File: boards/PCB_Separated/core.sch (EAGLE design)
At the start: 5 parts, among them U1 STM32F10XRXT6

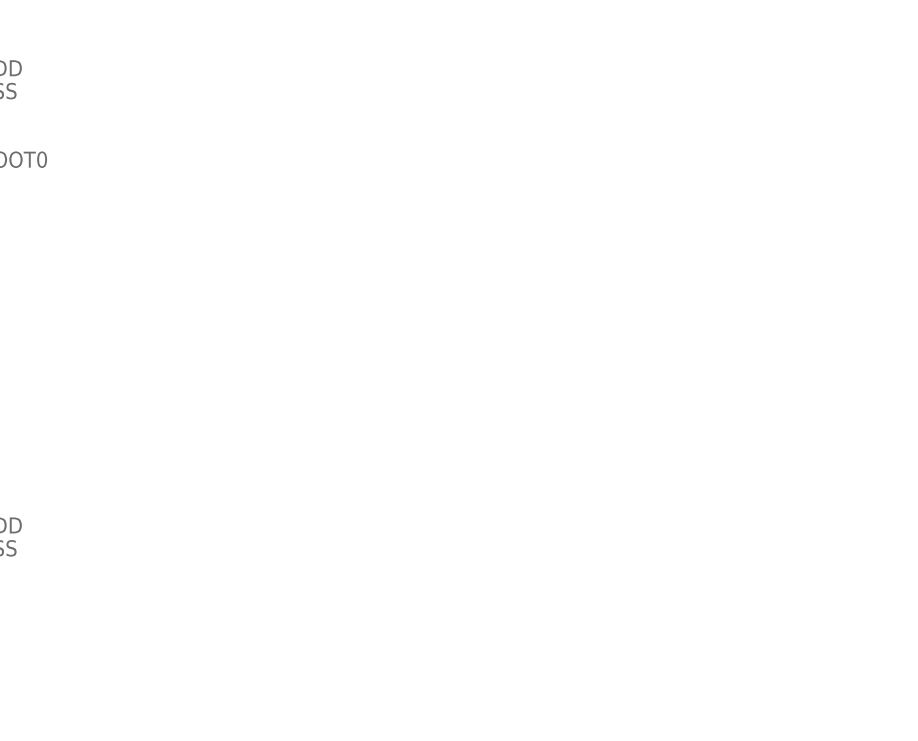
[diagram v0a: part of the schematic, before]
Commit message: Modify Board. Core and FTDI become one file
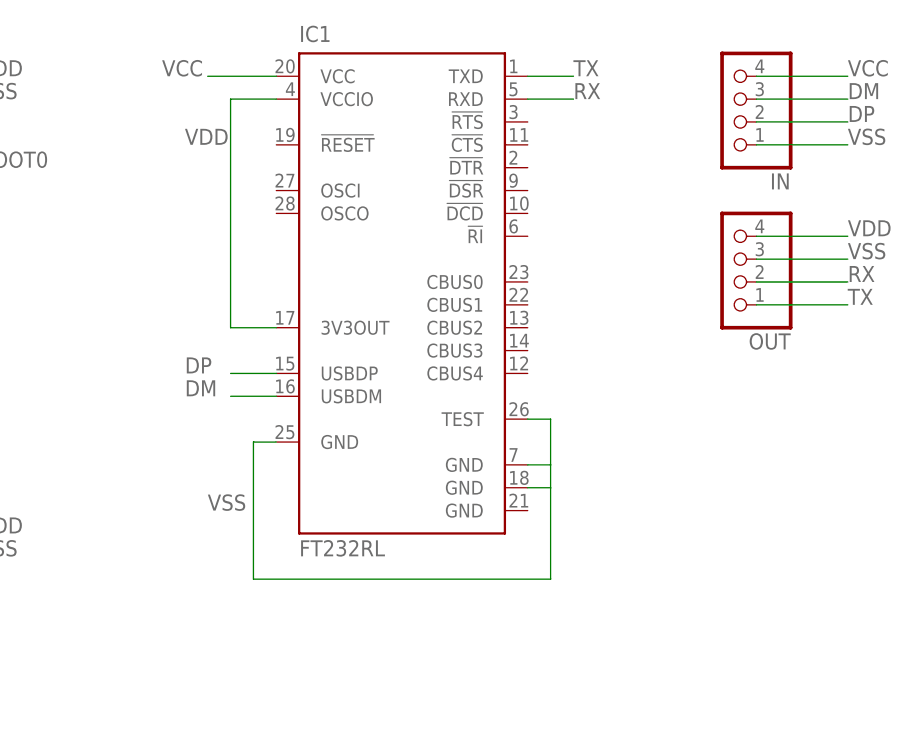
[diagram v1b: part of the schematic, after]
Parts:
- added IC1: FT232RL, ftdichip:FT232RL
- added IN, OUT: (no value), pinhead:PINHD-1X4
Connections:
- new net DM: IC1.USBDM, IN.3
- new net DP: IC1.USBDP, IN.2
- new net RX: IC1.RXD, OUT.2
- new net TX: IC1.TXD, OUT.1
- new net VCC: IC1.VCC, IN.4
- net VDD: now also IC1.3V3OUT, IC1.VCCIO, OUT.4
- net VSS: now also IC1.GND, IC1.GND@1, IC1.GND@A, IC1.TEST, IN.1, OUT.3
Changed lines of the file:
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@@
 <part name="JP3" library="pinhead" deviceset="PINHD-1X16" device=""/>
 <part name="JP4" library="pinhead" deviceset="PINHD-1X16" device=""/>
+<part name="IC1" library="ftdichip" deviceset="FT232R" device="L"/>
+<part name="IN" library="pinhead" deviceset="PINHD-1X4" device=""/>
+<part name="OUT" library="pinhead" deviceset="PINHD-1X4" device=""/>
 </parts>
 <sheets>
@@
 <instance part="JP3" gate="A" x="99.06" y="12.7" rot="R180"/>
 <instance part="JP4" gate="A" x="99.06" y="63.5" rot="R180"/>
+<instance part="IC1" gate="1" x="160.02" y="60.96"/>
+<instance part="IN" gate="A" x="198.12" y="81.28" rot="R180"/>
+<instance part="OUT" gate="A" x="198.12" y="63.5" rot="R180"/>
 </instances>
 <busses>
@@
 <label x="114.3" y="81.28" size="1.778" layer="95"/>
 </segment>
+<segment>
+<pinref part="IC1" gate="1" pin="GND@A"/>
+<wire x1="147.32" y1="43.18" x2="144.78" y2="43.18" width="0.1524" layer="91"/>
+<wire x1="144.78" y1="43.18" x2="144.78" y2="27.94" width="0.1524" layer="91"/>
+<wire x1="144.78" y1="27.94" x2="177.8" y2="27.94" width="0.1524" layer="91"/>
+<wire x1="177.8" y1="27.94" x2="177.8" y2="38.1" width="0.1524" layer="91"/>
+<pinref part="IC1" gate="1" pin="TEST"/>
+<wire x1="177.8" y1="38.1" x2="177.8" y2="40.64" width="0.1524" layer="91"/>
+<wire x1="177.8" y1="40.64" x2="177.8" y2="45.72" width="0.1524" layer="91"/>
+<wire x1="177.8" y1="45.72" x2="175.26" y2="45.72" width="0.1524" layer="91"/>
+<pinref part="IC1" gate="1" pin="GND"/>
+<wire x1="175.26" y1="40.64" x2="177.8" y2="40.64" width="0.1524" layer="91"/>
+<pinref part="IC1" gate="1" pin="GND@1"/>
+<wire x1="175.26" y1="38.1" x2="177.8" y2="38.1" width="0.1524" layer="91"/>
+<label x="139.7" y="35.56" size="1.778" layer="95"/>
+</segment>
+<segment>
+<pinref part="IN" gate="A" pin="1"/>
+<wire x1="200.66" y1="76.2" x2="210.82" y2="76.2" width="0.1524" layer="91"/>
+<label x="210.82" y="76.2" size="1.778" layer="95"/>
+</segment>
+<segment>
+<pinref part="OUT" gate="A" pin="3"/>
+<wire x1="200.66" y1="63.5" x2="210.82" y2="63.5" width="0.1524" layer="91"/>
+<label x="210.82" y="63.5" size="1.778" layer="95"/>
+</segment>
 </net>
 <net name="VDD" class="0">
@@
 <label x="114.3" y="83.82" size="1.778" layer="95"/>
 </segment>
+<segment>
+<pinref part="IC1" gate="1" pin="3V3OUT"/>
+<wire x1="147.32" y1="55.88" x2="142.24" y2="55.88" width="0.1524" layer="91"/>
+<wire x1="142.24" y1="55.88" x2="142.24" y2="81.28" width="0.1524" layer="91"/>
+<pinref part="IC1" gate="1" pin="VCCIO"/>
+<wire x1="142.24" y1="81.28" x2="147.32" y2="81.28" width="0.1524" layer="91"/>
+<label x="137.16" y="76.2" size="1.778" layer="95"/>
+</segment>
+<segment>
+<pinref part="OUT" gate="A" pin="4"/>
+<wire x1="200.66" y1="66.04" x2="210.82" y2="66.04" width="0.1524" layer="91"/>
+<label x="210.82" y="66.04" size="1.778" layer="95"/>
+</segment>
 </net>
 <net name="P14" class="0">
@@
 </segment>
 </net>
+<net name="VCC" class="0">
+<segment>
+<pinref part="IC1" gate="1" pin="VCC"/>
+<wire x1="147.32" y1="83.82" x2="139.7" y2="83.82" width="0.1524" layer="91"/>
+<label x="134.62" y="83.82" size="1.778" layer="95"/>
+</segment>
+<segment>
+<pinref part="IN" gate="A" pin="4"/>
+<wire x1="200.66" y1="83.82" x2="210.82" y2="83.82" width="0.1524" layer="91"/>
+<label x="210.82" y="83.82" size="1.778" layer="95"/>
+</segment>
+</net>
+<net name="DP" class="0">
+<segment>
+<pinref part="IC1" gate="1" pin="USBDP"/>
+<wire x1="147.32" y1="50.8" x2="142.24" y2="50.8" width="0.1524" layer="91"/>
+<label x="137.16" y="50.8" size="1.778" layer="95"/>
+</segment>
+<segment>
+<pinref part="IN" gate="A" pin="2"/>
+<wire x1="200.66" y1="78.74" x2="210.82" y2="78.74" width="0.1524" layer="91"/>
+<label x="210.82" y="78.74" size="1.778" layer="95"/>
+</segment>
+</net>
+<net name="DM" class="0">
+<segment>
+<pinref part="IC1" gate="1" pin="USBDM"/>
+<wire x1="147.32" y1="48.26" x2="142.24" y2="48.26" width="0.1524" layer="91"/>
+<label x="137.16" y="48.26" size="1.778" layer="95"/>
+</segment>
+<segment>
+<pinref part="IN" gate="A" pin="3"/>
+<wire x1="200.66" y1="81.28" x2="210.82" y2="81.28" width="0.1524" layer="91"/>
+<label x="210.82" y="81.28" size="1.778" layer="95"/>
+</segment>
+</net>
+<net name="TX" class="0">
+<segment>
+<pinref part="IC1" gate="1" pin="TXD"/>
+<wire x1="175.26" y1="83.82" x2="180.34" y2="83.82" width="0.1524" layer="91"/>
+<label x="180.34" y="83.82" size="1.778" layer="95"/>
+</segment>
+<segment>
+<pinref part="OUT" gate="A" pin="1"/>
+<wire x1="200.66" y1="58.42" x2="210.82" y2="58.42" width="0.1524" layer="91"/>
+<label x="210.82" y="58.42" size="1.778" layer="95"/>
+</segment>
+</net>
+<net name="RX" class="0">
+<segment>
+<pinref part="IC1" gate="1" pin="RXD"/>
+<wire x1="175.26" y1="81.28" x2="180.34" y2="81.28" width="0.1524" layer="91"/>
+<label x="180.34" y="81.28" size="1.778" layer="95"/>
+</segment>
+<segment>
+<pinref part="OUT" gate="A" pin="2"/>
+<wire x1="200.66" y1="60.96" x2="210.82" y2="60.96" width="0.1524" layer="91"/>
+<label x="210.82" y="60.96" size="1.778" layer="95"/>
+</segment>
+</net>

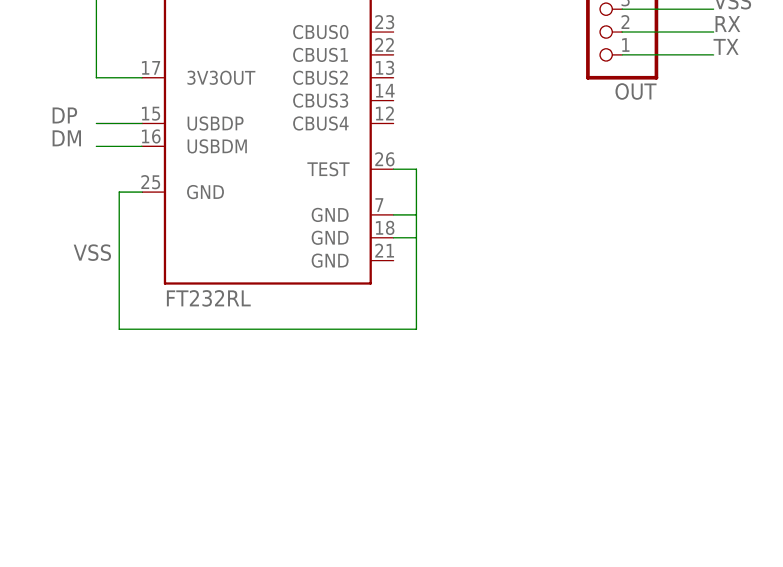
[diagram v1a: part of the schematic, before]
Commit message: -delete a useless sch pics -add ecu io pins diagram -add a GND to VSS line on FTDI. Hopefully internally connected with other GND pins -progress new separated ecu board.
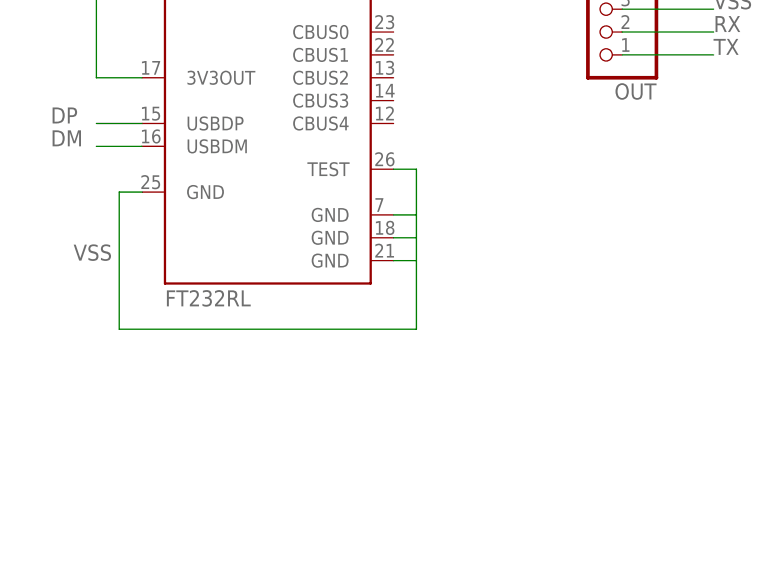
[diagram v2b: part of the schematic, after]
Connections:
- net VSS: now also IC1.GND@2
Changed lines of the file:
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@@
 <wire x1="144.78" y1="43.18" x2="144.78" y2="27.94" width="0.1524" layer="91"/>
 <wire x1="144.78" y1="27.94" x2="177.8" y2="27.94" width="0.1524" layer="91"/>
-<wire x1="177.8" y1="27.94" x2="177.8" y2="38.1" width="0.1524" layer="91"/>
+<wire x1="177.8" y1="27.94" x2="177.8" y2="35.56" width="0.1524" layer="91"/>
 <pinref part="IC1" gate="1" pin="TEST"/>
+<wire x1="177.8" y1="35.56" x2="177.8" y2="38.1" width="0.1524" layer="91"/>
 <wire x1="177.8" y1="38.1" x2="177.8" y2="40.64" width="0.1524" layer="91"/>
 <wire x1="177.8" y1="40.64" x2="177.8" y2="45.72" width="0.1524" layer="91"/>
@@
 <wire x1="175.26" y1="38.1" x2="177.8" y2="38.1" width="0.1524" layer="91"/>
 <label x="139.7" y="35.56" size="1.778" layer="95"/>
+<pinref part="IC1" gate="1" pin="GND@2"/>
+<wire x1="175.26" y1="35.56" x2="177.8" y2="35.56" width="0.1524" layer="91"/>
 </segment>
 <segment>
